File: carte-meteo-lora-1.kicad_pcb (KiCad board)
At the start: 2 copper layers, 119 parts, among them J1 TC2030, J2 Conn_01x04, J3 Conn_01x04, J4 Conn_Coaxial, J5 USB_C_Receptacle_USB2.0_14P, J6 Solar_Cell, J7 Conn_01x02, J8 Battery_Cell, Q1 AO4882, Q2 AO4882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

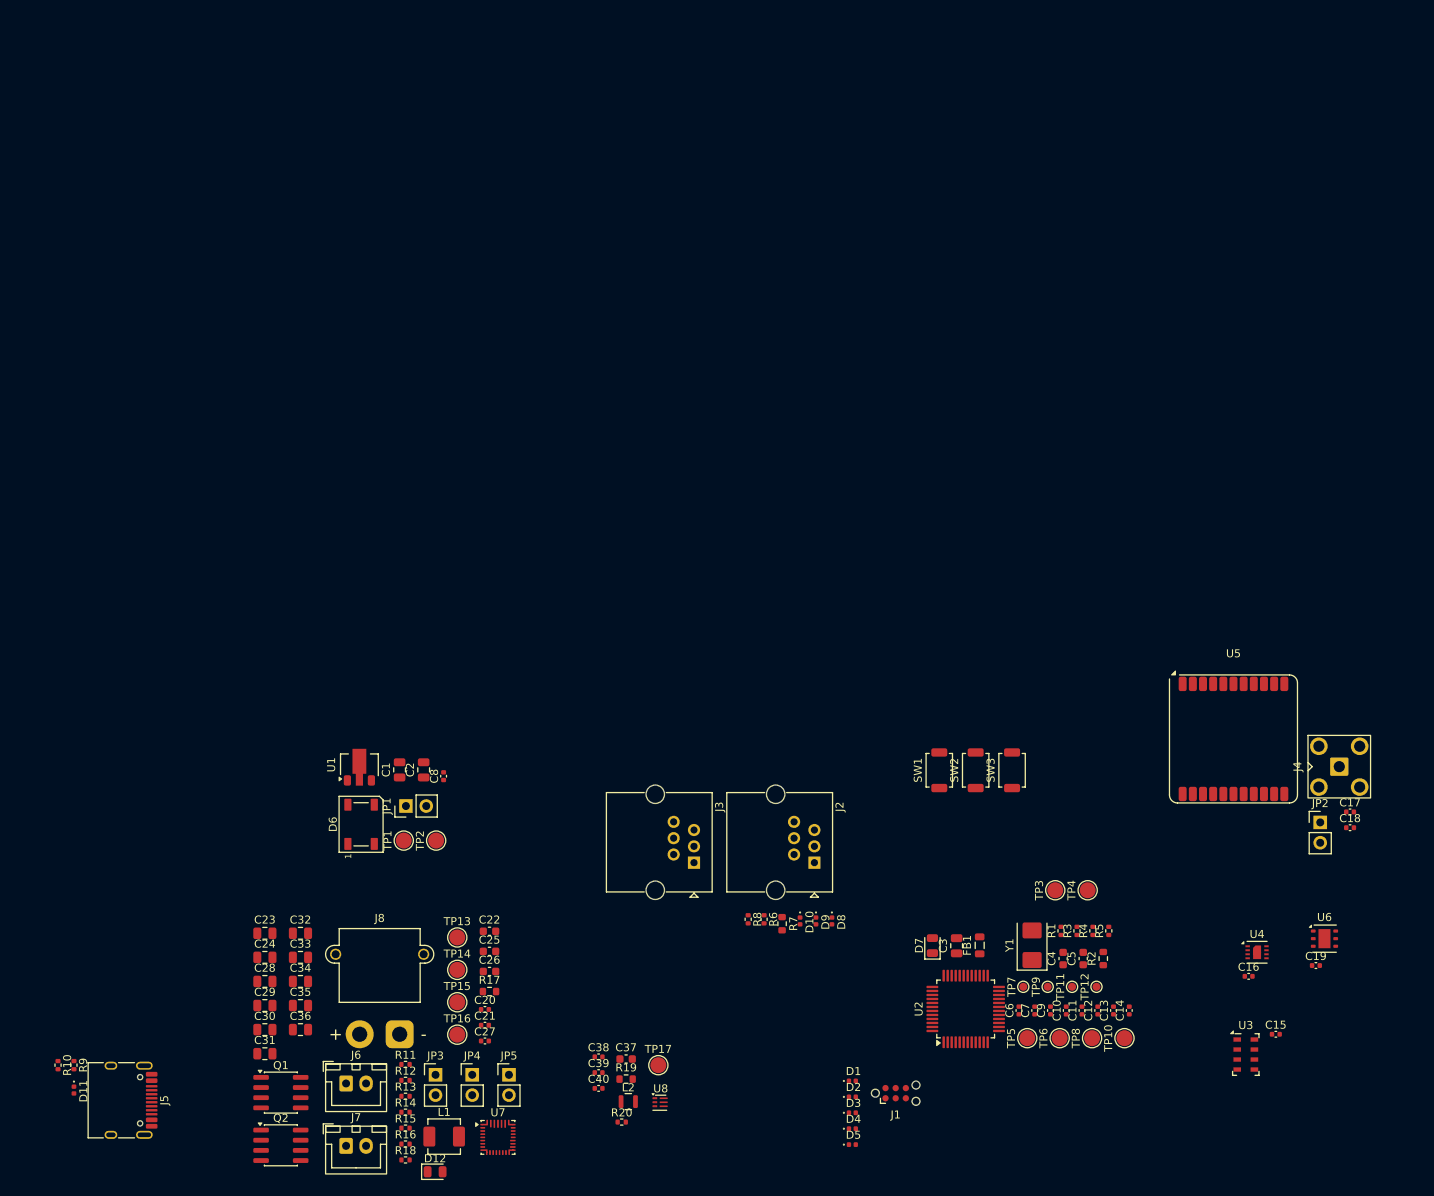
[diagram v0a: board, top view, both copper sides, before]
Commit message: pcb: add usb layout
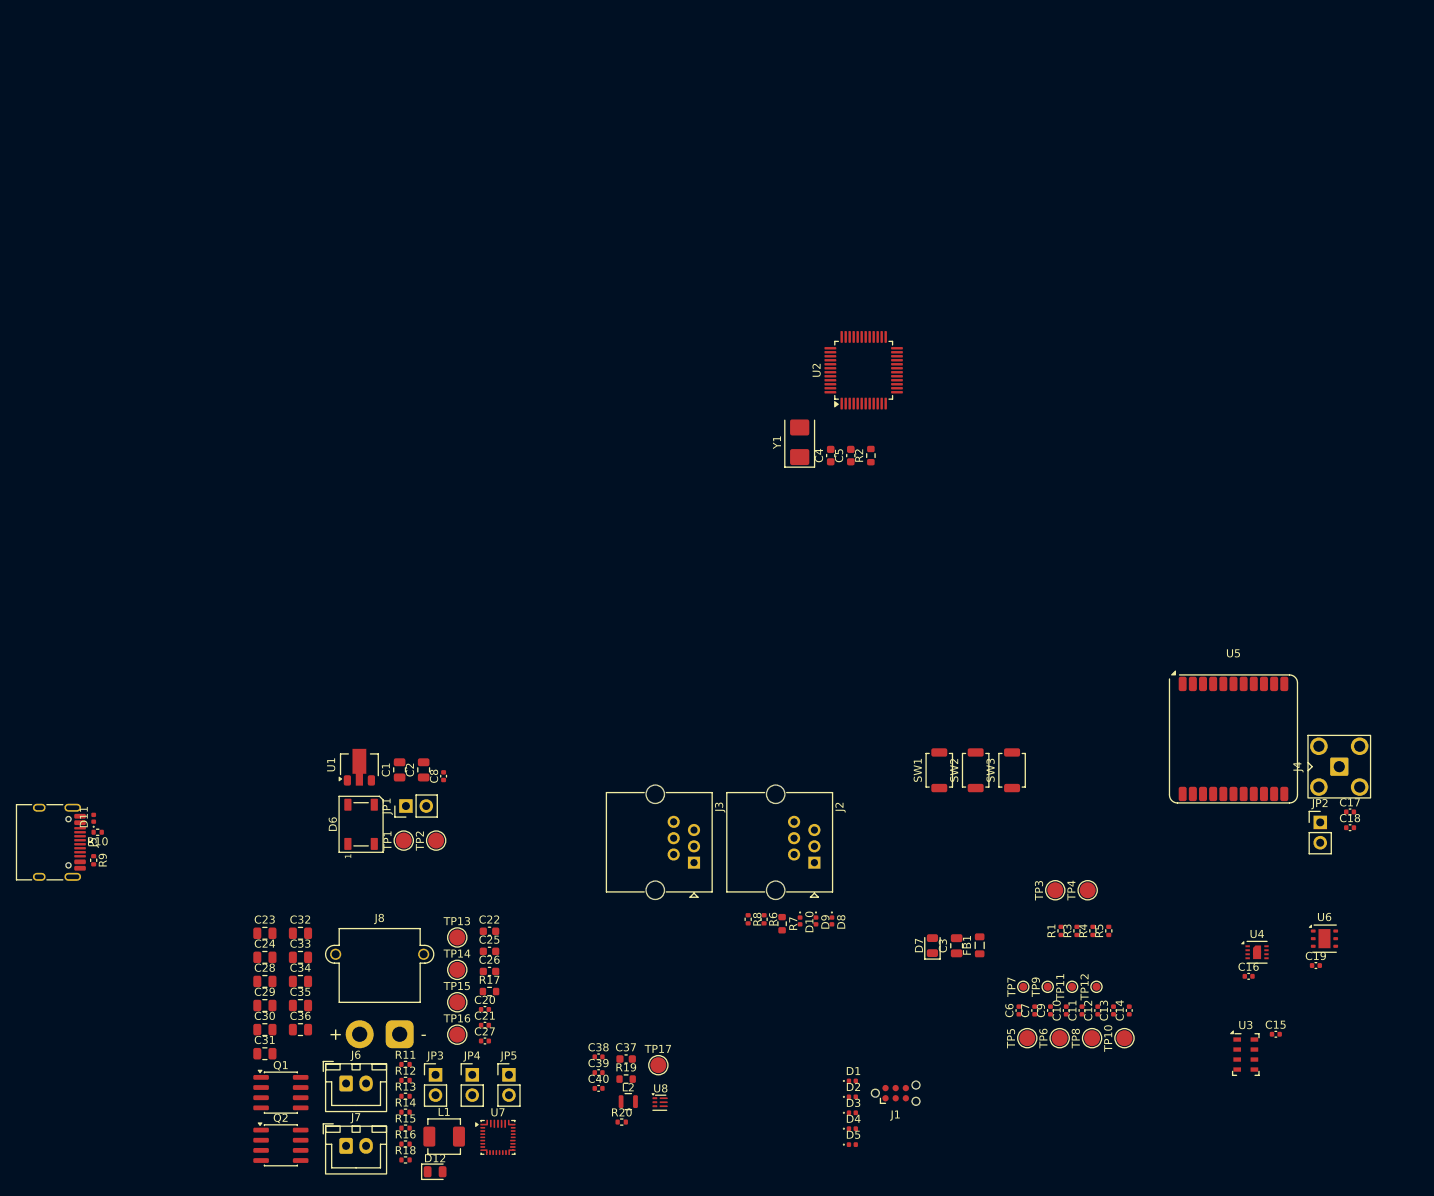
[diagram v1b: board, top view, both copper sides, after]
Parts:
- moved U2 80.8 mm to (138.0, 69.0)
- moved Y1 69.3 mm to (130.0, 78.0)
- moved C4 69.3 mm to (133.9, 79.7)
- moved C5 69.3 mm to (136.4, 79.7)
- moved R2 69.3 mm to (138.9, 79.7)
- moved D11 34.1 mm to (41.8, 125.0), turned to 90 degrees
- moved J5 33.5 mm to (36.0, 128.0)
- moved R10 29.5 mm to (42.2, 126.8), turned to 180 degrees
- moved R9 25.7 mm to (41.8, 130.2)
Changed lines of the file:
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@@
 	(footprint "Capacitor_SMD:C_0603_1608Metric"
 		(layer "F.Cu")
-		(at 165.44 142.5375 90)
+		(at 136.39 79.665 90)
 		(descr "Capacitor SMD 0603 (1608 Metric), square (rectangular) end terminal, IPC-7351 nominal, (Body size source: IPC-SM-782 page 76, https://www.pcb-3d.com/wordpress/wp-content/uploads/ipc-sm-782a_amendment_1_and_2.pdf)")
 		(tags "capacitor")
@@
 	(footprint "Package_QFP:LQFP-48_7x7mm_P0.5mm"
 		(layer "F.Cu")
-		(at 150.75 148.8375 90)
+		(at 138 69 90)
 		(descr "LQFP, 48 Pin (JEDEC MS-026 variation BBC, 1.40mm body thickness, https://www.jedec.org/document_search?search_api_views_fulltext=MS-026, https://www.analog.com/media/en/package-pcb-resources/package/pkg_pdf/ltc-legacy-lqfp/05081760_a_lx48.pdf)")
 		(tags "LQFP QFP CASE-932AA CASE-932-03 C48-1 C48-2 C48-3 C48-5 C48-6 C48-6C PT0048A")
@@
 	(footprint "Resistor_SMD:R_0402_1005Metric"
 		(layer "F.Cu")
-		(at 39.285 155.86 -90)
+		(at 41.75 130.25 -90)
 		(descr "Resistor SMD 0402 (1005 Metric), square (rectangular) end terminal, IPC-7351 nominal, (Body size source: IPC-SM-782 page 72, https://www.pcb-3d.com/wordpress/wp-content/uploads/ipc-sm-782a_amendment_1_and_2.pdf)")
 		(tags "resistor")
@@
 	(footprint "GLCS:Diode_DFN1006"
 		(layer "F.Cu")
-		(at 39.285 158.975 -90)
+		(at 41.75 125 90)
 		(descr "Diode SMD 0402 (1005 Metric), square (rectangular) end terminal, IPC-7351 nominal, (Body size source: http://www.tortai-tech.com/upload/download/2011102023233369053.pdf), generated with kicad-footprint-generator")
 		(tags "diode")
@@
 		)
 		(property "Basic" "E"
-			(at 0 0 270)
+			(at 0 0 90)
 			(unlocked yes)
 			(layer "F.Fab")
@@
 		)
 		(property "JLCPCB Part #" "C22395519"
-			(at 0 0 270)
+			(at 0 0 90)
 			(unlocked yes)
 			(layer "F.Fab")
@@
 		)
 		(property "Manufacturer" "hongjiacheng"
-			(at 0 0 270)
+			(at 0 0 90)
 			(unlocked yes)
 			(layer "F.Fab")
@@
 		)
 		(property "Manufacturer Part Number" "H5VU10U"
-			(at 0 0 270)
+			(at 0 0 90)
 			(unlocked yes)
 			(layer "F.Fab")
@@
 		)
 		(fp_line
-			(start -0.86 0.47)
-			(end -0.86 -0.47)
+			(start 0.87 -0.47)
+			(end 0.87 0.47)
 			(stroke
 				(width 0.05)
@@
 		)
 		(fp_line
-			(start 0.87 0.47)
-			(end -0.86 0.47)
+			(start -0.86 -0.47)
+			(end 0.87 -0.47)
 			(stroke
 				(width 0.05)
@@
 		)
 		(fp_line
-			(start -0.86 -0.47)
-			(end 0.87 -0.47)
+			(start 0.87 0.47)
+			(end -0.86 0.47)
 			(stroke
 				(width 0.05)
@@
 		)
 		(fp_line
-			(start 0.87 -0.47)
-			(end 0.87 0.47)
+			(start -0.86 0.47)
+			(end -0.86 -0.47)
 			(stroke
 				(width 0.05)
@@
 		)
 		(fp_line
-			(start -0.56 0.25)
-			(end -0.56 -0.25)
+			(start 0.44 -0.25)
+			(end 0.44 0.25)
 			(stroke
 				(width 0.1)
@@
 		)
 		(fp_line
-			(start -0.46 0.25)
-			(end -0.46 -0.25)
+			(start -0.56 -0.25)
+			(end 0.44 -0.25)
 			(stroke
 				(width 0.1)
@@
 		)
 		(fp_line
-			(start -0.36 0.25)
-			(end -0.36 -0.25)
+			(start 0.44 0.25)
+			(end -0.56 0.25)
 			(stroke
 				(width 0.1)
@@
 		)
 		(fp_line
-			(start 0.44 0.25)
-			(end -0.56 0.25)
+			(start -0.36 0.25)
+			(end -0.36 -0.25)
 			(stroke
 				(width 0.1)
@@
 		)
 		(fp_line
-			(start -0.56 -0.25)
-			(end 0.44 -0.25)
+			(start -0.46 0.25)
+			(end -0.46 -0.25)
 			(stroke
 				(width 0.1)
@@
 		)
 		(fp_line
-			(start 0.44 -0.25)
-			(end 0.44 0.25)
+			(start -0.56 0.25)
+			(end -0.56 -0.25)
 			(stroke
 				(width 0.1)
@@
 		)
 		(pad "1" smd roundrect
-			(at -0.425 0 270)
+			(at -0.425 0 90)
 			(size 0.55 0.6)
 			(layers "F.Cu" "F.Mask" "F.Paste")
@@
 		)
 		(pad "2" smd roundrect
-			(at 0.425 0 270)
+			(at 0.425 0 90)
 			(size 0.55 0.6)
 			(layers "F.Cu" "F.Mask" "F.Paste")
@@
 	(footprint "Resistor_SMD:R_0603_1608Metric"
 		(layer "F.Cu")
-		(at 167.95 142.5375 90)
+		(at 138.9 79.665 90)
 		(descr "Resistor SMD 0603 (1608 Metric), square (rectangular) end terminal, IPC-7351 nominal, (Body size source: IPC-SM-782 page 72, https://www.pcb-3d.com/wordpress/wp-content/uploads/ipc-sm-782a_amendment_1_and_2.pdf)")
 		(tags "resistor")
@@
 	(footprint "Capacitor_SMD:C_0603_1608Metric"
 		(layer "F.Cu")
-		(at 162.93 142.5375 90)
+		(at 133.88 79.665 90)
 		(descr "Capacitor SMD 0603 (1608 Metric), square (rectangular) end terminal, IPC-7351 nominal, (Body size source: IPC-SM-782 page 76, https://www.pcb-3d.com/wordpress/wp-content/uploads/ipc-sm-782a_amendment_1_and_2.pdf)")
 		(tags "capacitor")
@@
 	(footprint "Resistor_SMD:R_0402_1005Metric"
 		(layer "F.Cu")
-		(at 37.295 155.86 -90)
+		(at 42.25 126.75 180)
 		(descr "Resistor SMD 0402 (1005 Metric), square (rectangular) end terminal, IPC-7351 nominal, (Body size source: IPC-SM-782 page 72, https://www.pcb-3d.com/wordpress/wp-content/uploads/ipc-sm-782a_amendment_1_and_2.pdf)")
 		(tags "resistor")
 		(property "Reference" "R10"
-			(at 0 -1.17 90)
+			(at 0 -1.17 0)
 			(layer "F.SilkS")
 			(effects
@@
 		)
 		(property "Value" "5k1"
-			(at 0 1.17 90)
+			(at 0 1.17 0)
 			(layer "F.Fab")
 			(effects
@@
 		)
 		(property "Datasheet" ""
-			(at 0 0 90)
+			(at 0 0 0)
 			(layer "F.Fab")
 			(hide yes)
@@
 		)
 		(property "Description" "Resistor"
-			(at 0 0 90)
+			(at 0 0 0)
 			(layer "F.Fab")
 			(hide yes)
@@
 		)
 		(property "KiLib_Generator" "SMD_2terminal_chip_molded"
-			(at 0 0 90)
+			(at 0 0 0)
 			(layer "F.SilkS")
 			(hide yes)
@@
 		)
 		(property "Manufacturer" "Uniroyal Elec"
-			(at 0 0 270)
+			(at 0 0 180)
 			(unlocked yes)
 			(layer "F.Fab")
@@
 		)
 		(property "Manufacturer Part Number" "0402WGF5101TCE"
-			(at 0 0 270)
+			(at 0 0 180)
 			(unlocked yes)
 			(layer "F.Fab")
@@
 		)
 		(property "Basic" "Y"
-			(at 0 0 270)
+			(at 0 0 180)
 			(unlocked yes)
 			(layer "F.Fab")
@@
 		)
 		(property "JLCPCB Part #" "C25905"
-			(at 0 0 270)
+			(at 0 0 180)
 			(unlocked yes)
 			(layer "F.Fab")
@@
 		)
 		(fp_text user "${REFERENCE}"
-			(at 0 0 90)
+			(at 0 0 0)
 			(layer "F.Fab")
 			(effects
@@
 		)
 		(pad "1" smd roundrect
-			(at -0.51 0 270)
+			(at -0.51 0 180)
 			(size 0.54 0.64)
 			(layers "F.Cu" "F.Mask" "F.Paste")
@@
 		)
 		(pad "2" smd roundrect
-			(at 0.51 0 270)
+			(at 0.51 0 180)
 			(size 0.54 0.64)
 			(layers "F.Cu" "F.Mask" "F.Paste")
@@
 	(footprint "Connector_USB:USB_C_Receptacle_HRO_TYPE-C-31-M-12"
 		(layer "F.Cu")
-		(at 44.955 160.25 -90)
+		(at 36 128 -90)
 		(descr "USB Type-C receptacle for USB 2.0 and PD, http://www.krhro.com/uploads/soft/180320/1-1P320120243.pdf")
 		(tags "usb usb-c 2.0 pd")
@@
 	(footprint "Crystal:Crystal_SMD_5032-2Pin_5.0x3.2mm"
 		(layer "F.Cu")
-		(at 159.05 140.8725 90)
+		(at 130 78 90)
 		(descr "SMD2520/2, Crystal, 5.0x3.2mm package, SMD, http://www.icbase.com/File/PDF/HKC/HKC00061008.pdf")
 		(property "Reference" "Y1"

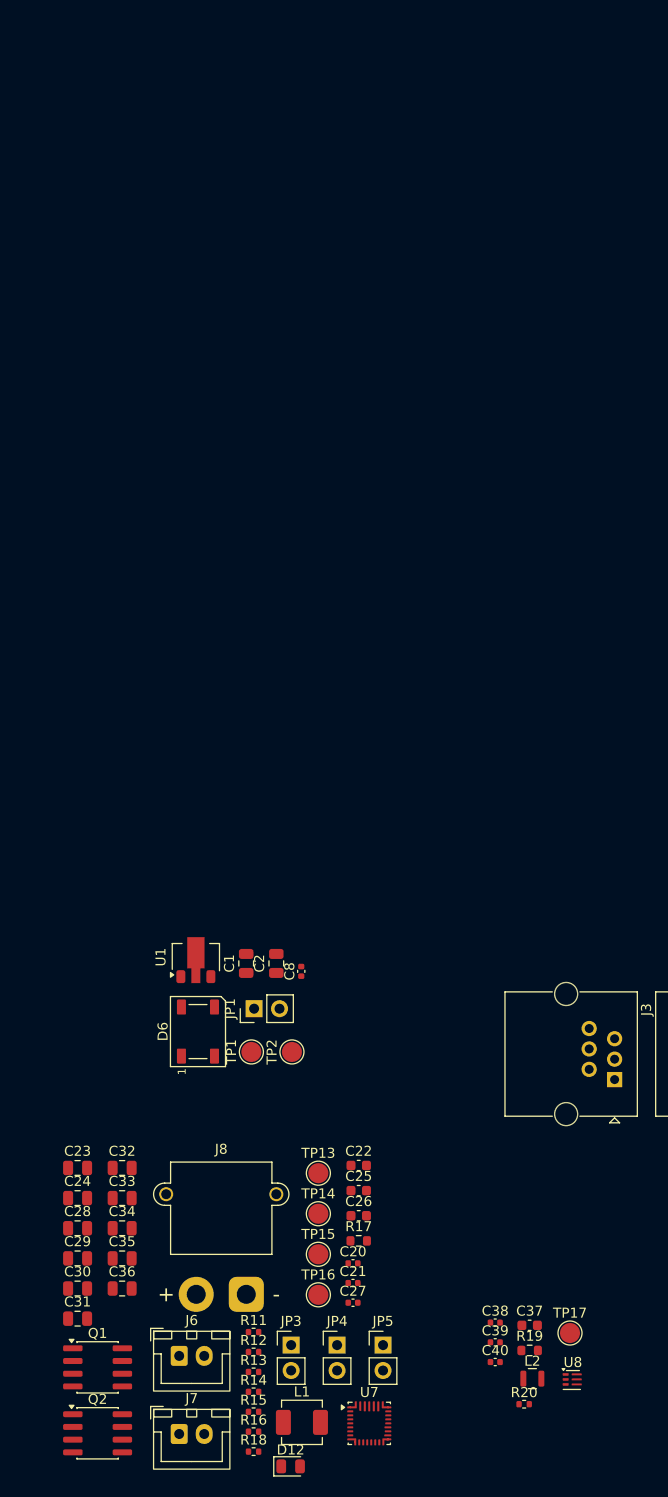
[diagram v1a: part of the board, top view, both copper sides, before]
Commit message: pcb: add solar charger layout
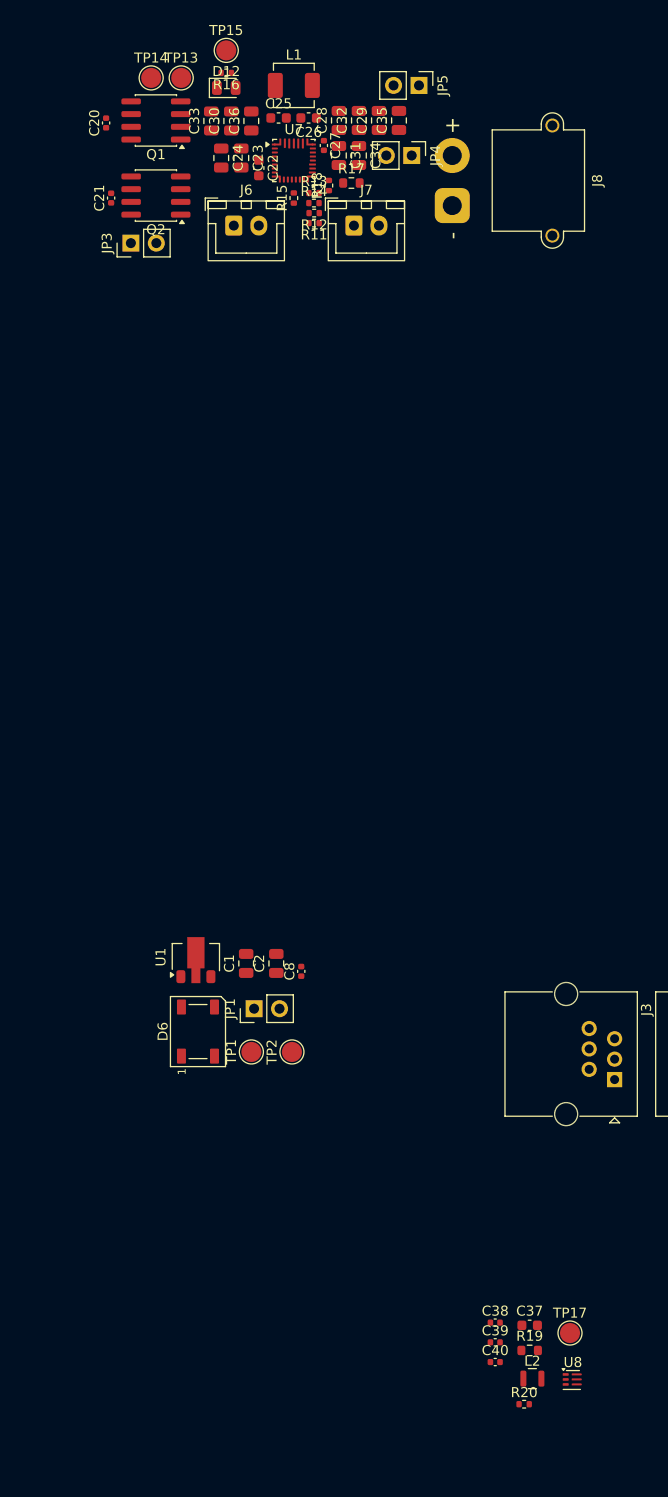
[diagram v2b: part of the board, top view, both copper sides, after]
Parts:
- removed TP16: TestPoint, TestPoint:TestPoint_Pad_D2.0mm
- moved D12 137.8 mm to (78.0, 31.5)
- moved R16 135.7 mm to (78.0, 30.0), turned to 180 degrees
- moved L1 133.5 mm to (84.8, 31.2)
- moved R18 126.7 mm to (88.2, 41.2), turned to 90 degrees
- moved U7 126.4 mm to (84.8, 38.8)
- moved JP5 125.9 mm to (97.2, 31.2), turned to -90 degrees
- moved Q1 124.7 mm to (71.0, 34.8), turned to 180 degrees
- moved Q2 123.8 mm to (71.0, 42.2), turned to 180 degrees
- moved J7 122.0 mm to (90.8, 45.2)
- moved R15 121.3 mm to (84.8, 42.5), turned to 90 degrees
- moved TP15 120.6 mm to (78.0, 27.8)
- moved C31 119.1 mm to (89.2, 38.2), turned to -90 degrees
- moved JP4 119.1 mm to (96.5, 38.2), turned to -90 degrees
- moved R14 118.9 mm to (86.8, 43.0)
- moved R13 117.9 mm to (86.8, 42.0)
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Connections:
- C27 pad 2: GND -> Net-(J8--)
